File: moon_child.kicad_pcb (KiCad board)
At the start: 4 copper layers, 63.2 x 63.2 mm, 186 parts, among them J1 Motor0, J10 USB_C_Receptacle_USB2.0_14P, J2 Motor1, J3 Battery Input, J4 Micro_SD_Card_Det1, J5 Conn_01x04, J6 Conn_01x04, J7 Conn_02x05_Odd_Even, J8 Conn_01x03, J9 debug_probe, Q1 BSP613P, Q2 Q_NPN_BCE, SW1 SW_Omron_B3FS, U1 DRV8871DDA, U2 DRV8871DDA, U3 AP62250Z6, U4 IIM-42652, U5 BME280, U6 RP2350B-QFN80, U7 INA180A1, U8 16Mbit PSRAM, U9 16Mbit PSRAM, X1 ASE-12.000MHZ-L-C-T

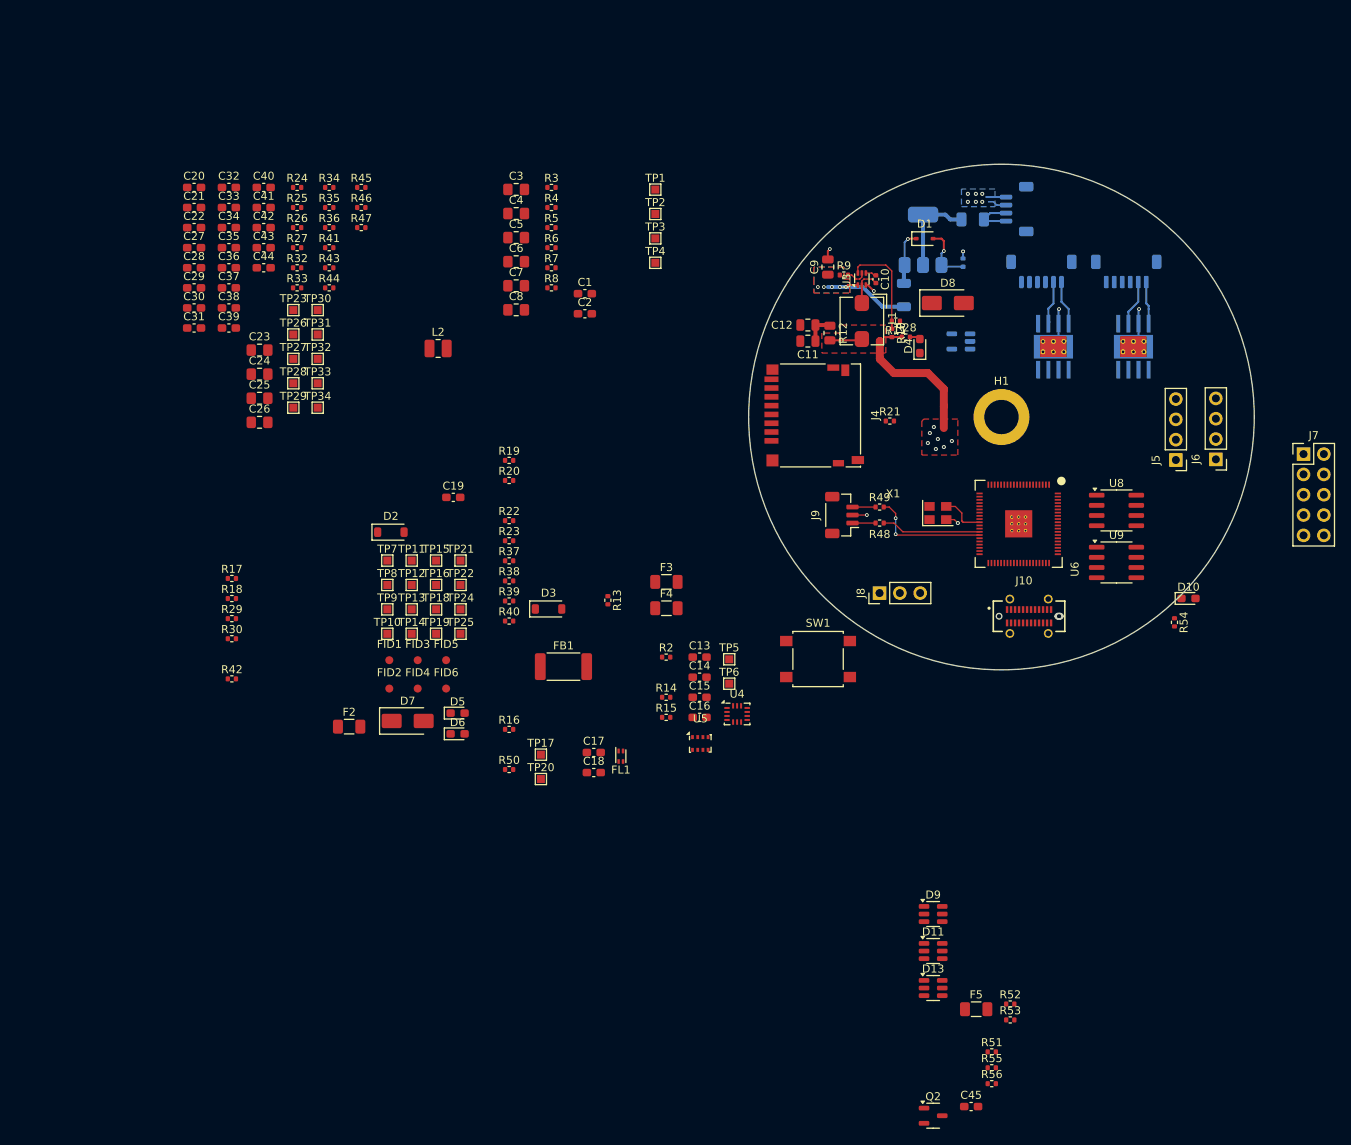
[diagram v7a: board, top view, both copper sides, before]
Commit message: QSPI routing
Added pretty sub-optimal qspi routing
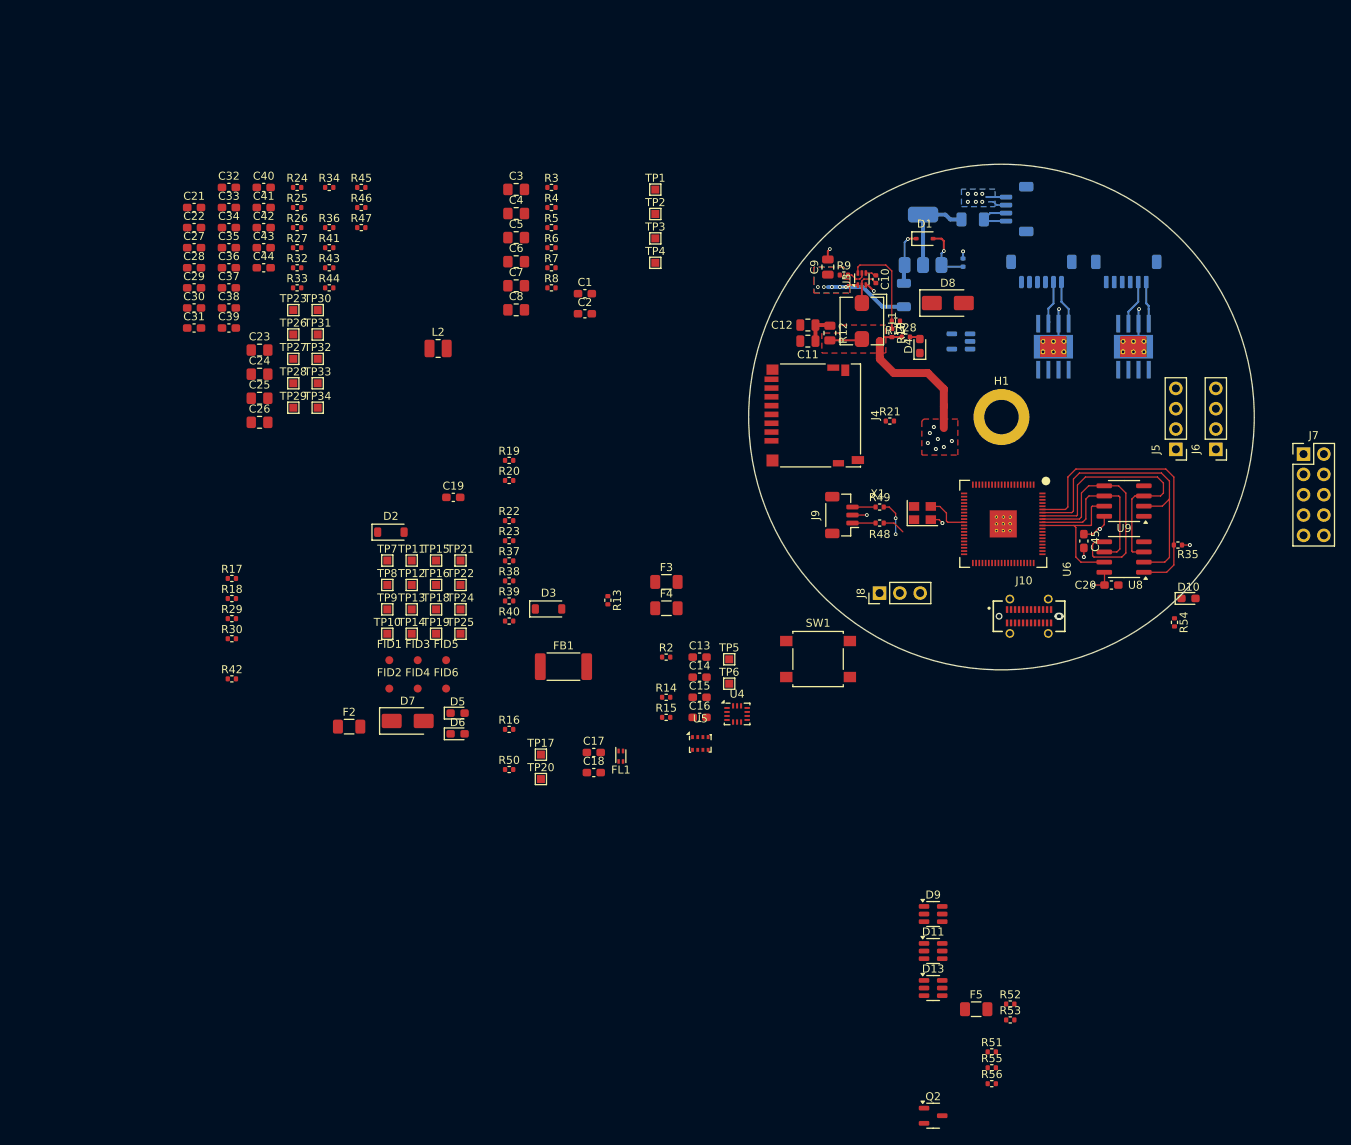
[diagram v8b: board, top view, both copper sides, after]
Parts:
- moved C20 125.0 mm to (172.9, 109.5)
- moved R35 114.2 mm to (181.3, 104.5), turned to 180 degrees
- moved C45 72.1 mm to (169.5, 104.0), turned to -90 degrees
- moved U9 7.73 mm to (174.5, 99.0), turned to 180 degrees
- moved U8 5.90 mm to (174.5, 106.0), turned to 180 degrees
- moved X1 1.93 mm to (149.3, 100.5)
- moved U6 1.93 mm to (159.4, 101.8)
- moved J5 1.33 mm to (181.0, 92.5)
- moved J6 1.25 mm to (186.0, 92.5)
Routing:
- net /raspi/QSPI_SD1: track 0.00 -> 37.2 mm
- net Net-(U6-QSPI_SS): track 0.00 -> 36.3 mm
- net /raspi/QSPI_SD2: track 0.00 -> 33.2 mm
- net /raspi/QSPI_SD0: track 0.00 -> 29.2 mm
- net /raspi/QSPI_SCLK: track 0.00 -> 21.2 mm
- net /raspi/QSPI_SD3: track 0.00 -> 17.9 mm
- net /raspi/SWDIO: track 15.1 -> 4.74 mm
- net /raspi/SWCLK: track 12.4 -> 2.85 mm
- net 3v3: track 23.0 -> 31.1 mm, vias 7 -> 10
- net GND: track 23.1 -> 24.2 mm, vias 13 -> 14
